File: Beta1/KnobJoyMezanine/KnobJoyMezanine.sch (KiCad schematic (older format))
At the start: 14 parts

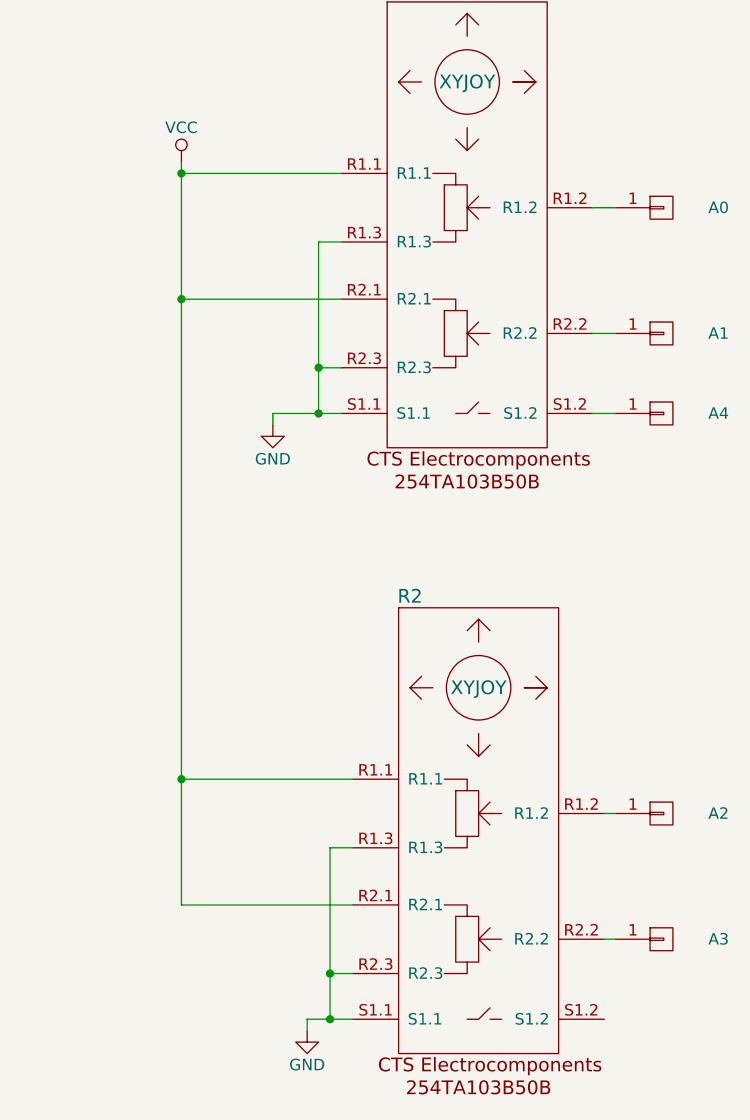
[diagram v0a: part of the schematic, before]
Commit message: Cloned 2CH Joy Mez and replaced a Joy with a knob (volume)
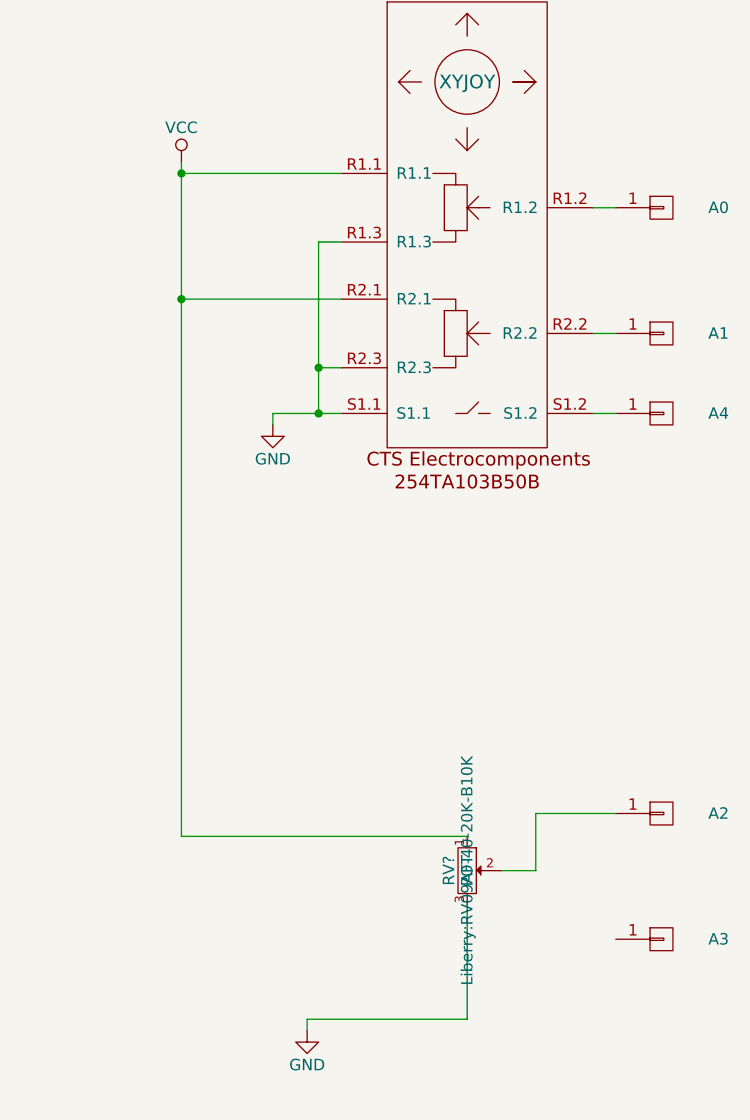
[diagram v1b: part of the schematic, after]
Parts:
- removed R2: XYJOY, Liberry:XY_JOY_254TA103B50B, symbol XYJOY
- added RV?: POT, Liberry:RV09AF-40-20K-B10K, symbol POT
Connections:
- net GND: now also RV?.3
- net VCC: now also RV?.1
- net at A2.1 (P1): now also RV?.2
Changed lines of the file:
@@
 LIBS:Zilog
 LIBS:believotron_wanderlust
-LIBS:JoyXYMezanine-cache
+LIBS:KnobJoyMezanine-cache
 EELAYER 25 0
 EELAYER END
@@
 $EndComp
 $Comp
-L GND #PWR2
+L GND #PWR01
 U 1 1 582E3FD0
 P 9000 1450
-F 0 "#PWR2" H 9000 1200 50  0001 C CNN
+F 0 "#PWR01" H 9000 1200 50  0001 C CNN
 F 1 "GND" H 9000 1300 50  0000 C CNN
 F 2 "" H 9000 1450 50  0000 C CNN
 F 3 "" H 9000 1450 50  0000 C CNN
 	1    9000 1450
-	1    0    0    -1
-$EndComp
-Wire Wire Line
-	8950 1200 9000 1200
-Wire Wire Line
-	9000 1200 9000 1450
-$Comp
-L XYJOY R2
-U 1 1 586B0449
-P 13850 5200
-F 0 "R2" H 13550 6150 60  0000 C CNN
-F 1 "XYJOY" H 13850 5750 60  0000 C CNN
-F 2 "Liberry:XY_JOY_254TA103B50B" H 13850 5750 60  0001 C CNN
-F 3 "" H 13850 5750 60  0001 C CNN
-	1    13850 5200
 	1    0    0    -1
 $EndComp
@@
 $EndComp
 $Comp
-L VCC #PWR1
+L VCC #PWR02
 U 1 1 586B0608
 P 9000 850
-F 0 "#PWR1" H 9000 700 50  0001 C CNN
+F 0 "#PWR02" H 9000 700 50  0001 C CNN
 F 1 "VCC" H 9000 1000 50  0000 C CNN
 F 2 "" H 9000 850 50  0000 C CNN
@@
 	1    0    0    -1
 $EndComp
-Wire Wire Line
-	9000 850  9000 900
-Wire Wire Line
-	9000 900  8950 900
-$Comp
-L GND #PWR4
+$Comp
+L GND #PWR03
 U 1 1 586B0C2D
 P 12950 3500
-F 0 "#PWR4" H 12950 3250 50  0001 C CNN
+F 0 "#PWR03" H 12950 3250 50  0001 C CNN
 F 1 "GND" H 12950 3350 50  0000 C CNN
 F 2 "" H 12950 3500 50  0000 C CNN
@@
 $EndComp
 $Comp
-L GND #PWR5
+L GND #PWR04
 U 1 1 586B0C53
 P 13100 6150
-F 0 "#PWR5" H 13100 5900 50  0001 C CNN
+F 0 "#PWR04" H 13100 5900 50  0001 C CNN
 F 1 "GND" H 13100 6000 50  0000 C CNN
 F 2 "" H 13100 6150 50  0000 C CNN
@@
 	1    0    0    -1
 $EndComp
-Wire Wire Line
-	13300 6100 13200 6100
-Wire Wire Line
-	13200 6100 13100 6100
-Wire Wire Line
-	13100 6100 13100 6150
-Wire Wire Line
-	12950 3450 13150 3450
-Wire Wire Line
-	13150 3450 13250 3450
-Wire Wire Line
-	12950 3450 12950 3500
-Wire Wire Line
-	14350 2550 14450 2550
-Wire Wire Line
-	14350 3100 14450 3100
-Wire Wire Line
-	14350 3450 14450 3450
 $Comp
 L CONN_01X01 NC0
@@
 $EndComp
 $Comp
-L VCC #PWR3
+L VCC #PWR05
 U 1 1 586B1045
 P 12550 2350
-F 0 "#PWR3" H 12550 2200 50  0001 C CNN
+F 0 "#PWR05" H 12550 2200 50  0001 C CNN
 F 1 "VCC" H 12550 2500 50  0000 C CNN
 F 2 "" H 12550 2350 50  0000 C CNN
@@
 	1    0    0    -1
 $EndComp
-Wire Wire Line
-	12550 2350 12550 2400
-Wire Wire Line
-	12550 2400 12550 2950
-Wire Wire Line
-	12550 2950 12550 5050
-Wire Wire Line
-	12550 5050 12550 5600
+$Comp
+L POT RV?
+U 1 1 586C01BF
+P 13800 5450
+F 0 "RV?" H 13800 5370 50  0000 C CNN
+F 1 "POT" H 13800 5450 50  0000 C CNN
+F 2 "Liberry:RV09AF-40-20K-B10K" H 13800 5450 50  0000 C CNN
+F 3 "" H 13800 5450 50  0000 C CNN
+	1    13800 5450
+	0    1    1    0
+$EndComp
+Wire Wire Line
+	8950 1200 9000 1200
+Wire Wire Line
+	9000 1200 9000 1450
+Wire Wire Line
+	9000 850  9000 900
+Wire Wire Line
+	9000 900  8950 900
+Wire Wire Line
+	13100 6100 13800 6100
+Wire Wire Line
+	13100 6100 13100 6150
+Wire Wire Line
+	12950 3450 13250 3450
+Wire Wire Line
+	12950 3450 12950 3500
+Wire Wire Line
+	14350 2550 14450 2550
+Wire Wire Line
+	14350 3100 14450 3100
+Wire Wire Line
+	14350 3450 14450 3450
 Wire Wire Line
 	12550 2400 13250 2400
@@
 	13250 2700 13150 2700
 Wire Wire Line
-	13150 2700 13150 3250
-Wire Wire Line
-	13150 3250 13150 3450
+	13150 2700 13150 3450
 Connection ~ 13150 3450
 Wire Wire Line
 	13250 3250 13150 3250
 Connection ~ 13150 3250
-Wire Wire Line
-	12550 5050 13300 5050
 Connection ~ 12550 2950
 Wire Wire Line
-	12550 5600 13300 5600
-Connection ~ 12550 5050
-Wire Wire Line
-	13300 5350 13200 5350
-Wire Wire Line
-	13200 5350 13200 5900
-Wire Wire Line
-	13200 5900 13200 6100
-Connection ~ 13200 6100
-Wire Wire Line
-	13300 5900 13200 5900
-Connection ~ 13200 5900
-Wire Wire Line
-	14400 5200 14450 5200
-Wire Wire Line
-	14400 5750 14450 5750
+	14100 5200 14450 5200
+Wire Wire Line
+	14100 5200 14100 5450
+Wire Wire Line
+	14100 5450 13950 5450
+Wire Wire Line
+	13800 6100 13800 5600
+Wire Wire Line
+	12550 5300 13800 5300
+Wire Wire Line
+	12550 2350 12550 5300
 $EndSCHEMATC

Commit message: Annotated component.
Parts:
- gave numbers to parts that had none: 1
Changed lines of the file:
@@
 $EndComp
 $Comp
-L POT RV?
+L POT RV1
 U 1 1 586C01BF
 P 13800 5450
-F 0 "RV?" H 13800 5370 50  0000 C CNN
+F 0 "RV1" H 13800 5370 50  0000 C CNN
 F 1 "POT" H 13800 5450 50  0000 C CNN
 F 2 "Liberry:RV09AF-40-20K-B10K" H 13800 5450 50  0000 C CNN
